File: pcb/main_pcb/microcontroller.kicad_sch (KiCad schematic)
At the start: 33 parts, among them J1 Conn_01x05, J10 Conn_01x06_Male, J11 Conn_01x04, J2 Conn_01x05, J3 Conn_01x05, J4 Conn_01x05, J5 Conn_01x05, J6 Conn_01x05, J7 Conn_01x04, J8 Conn_01x06_Male, J9 Conn_01x04, U1 LSM6DSO, U2 Teensy_4.1, U3 DRV8833

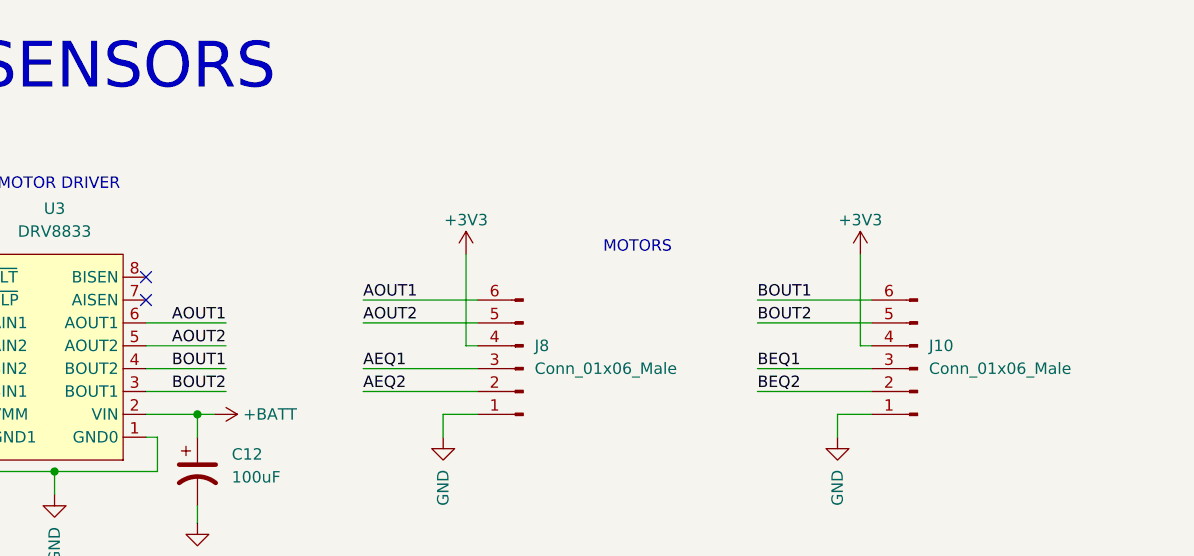
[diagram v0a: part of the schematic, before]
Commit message: Fix many DRC errors; correct motor B sig names
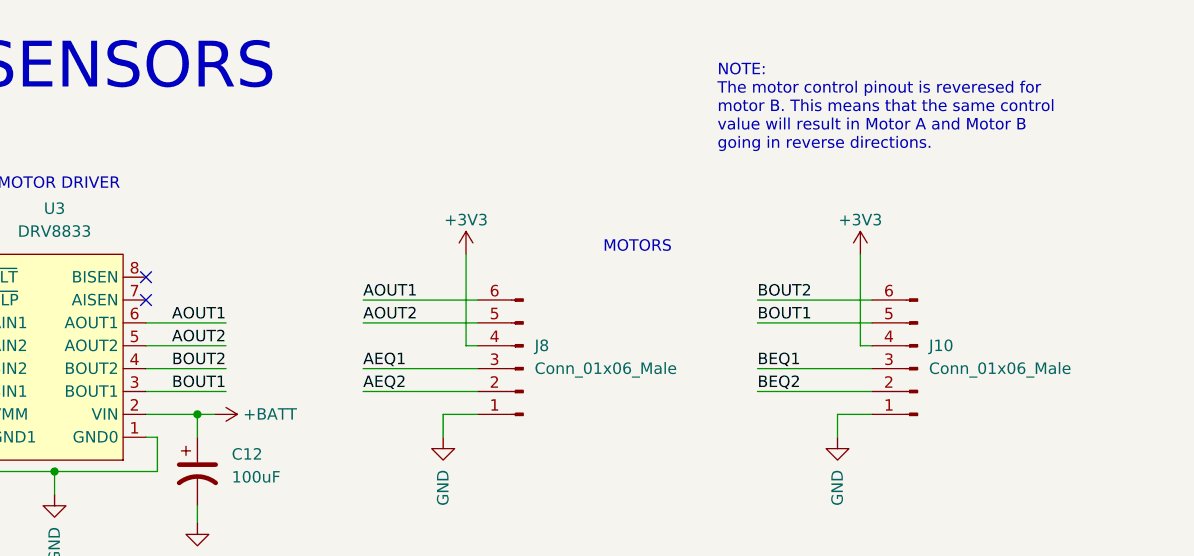
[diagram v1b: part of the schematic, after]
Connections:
- net BOUT1: now also J10.5 (Pin_5), U3.3 (BOUT1); no longer J10.6 (Pin_6), U3.4 (BOUT2)
- net BOUT2: now also J10.6 (Pin_6), U3.4 (BOUT2); no longer J10.5 (Pin_5), U3.3 (BOUT1)
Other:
- note added: "NOTE: The motor control pinout is reveresed for motor B. This means that the same control value will result in Motor A and Motor B going in reverse directions."
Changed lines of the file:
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@@
+    (effects (font (size 1.27 1.27)) (justify left bottom))
+  )
+  (text "NOTE:\nThe motor control pinout is reveresed for\nmotor B. This means that the same control\nvalue will result in Motor A and Motor B\ngoing in reverse directions. "
+    (at 230.505 33.655 0)
     (effects (font (size 1.27 1.27)) (justify left bottom))
   )
@@
     (effects (font (size 1.27 1.27)) (justify left bottom))
   )
-  (label "BOUT1" (at 234.95 50.165 0)
+  (label "BOUT2" (at 234.95 50.165 0)
     (effects (font (size 1.27 1.27)) (justify left bottom))
   )
@@
     (effects (font (size 1.27 1.27)) (justify right bottom))
   )
-  (label "BOUT1" (at 175.895 57.785 180)
+  (label "BOUT2" (at 175.895 57.785 180)
     (effects (font (size 1.27 1.27)) (justify right bottom))
   )
@@
     (effects (font (size 1.27 1.27)) (justify left bottom))
   )
-  (label "BOUT2" (at 234.95 52.705 0)
+  (label "BOUT1" (at 234.95 52.705 0)
     (effects (font (size 1.27 1.27)) (justify left bottom))
   )
@@
     (effects (font (size 1.27 1.27)) (justify right bottom))
   )
-  (label "BOUT2" (at 175.895 60.325 180)
+  (label "BOUT1" (at 175.895 60.325 180)
     (effects (font (size 1.27 1.27)) (justify right bottom))
   )

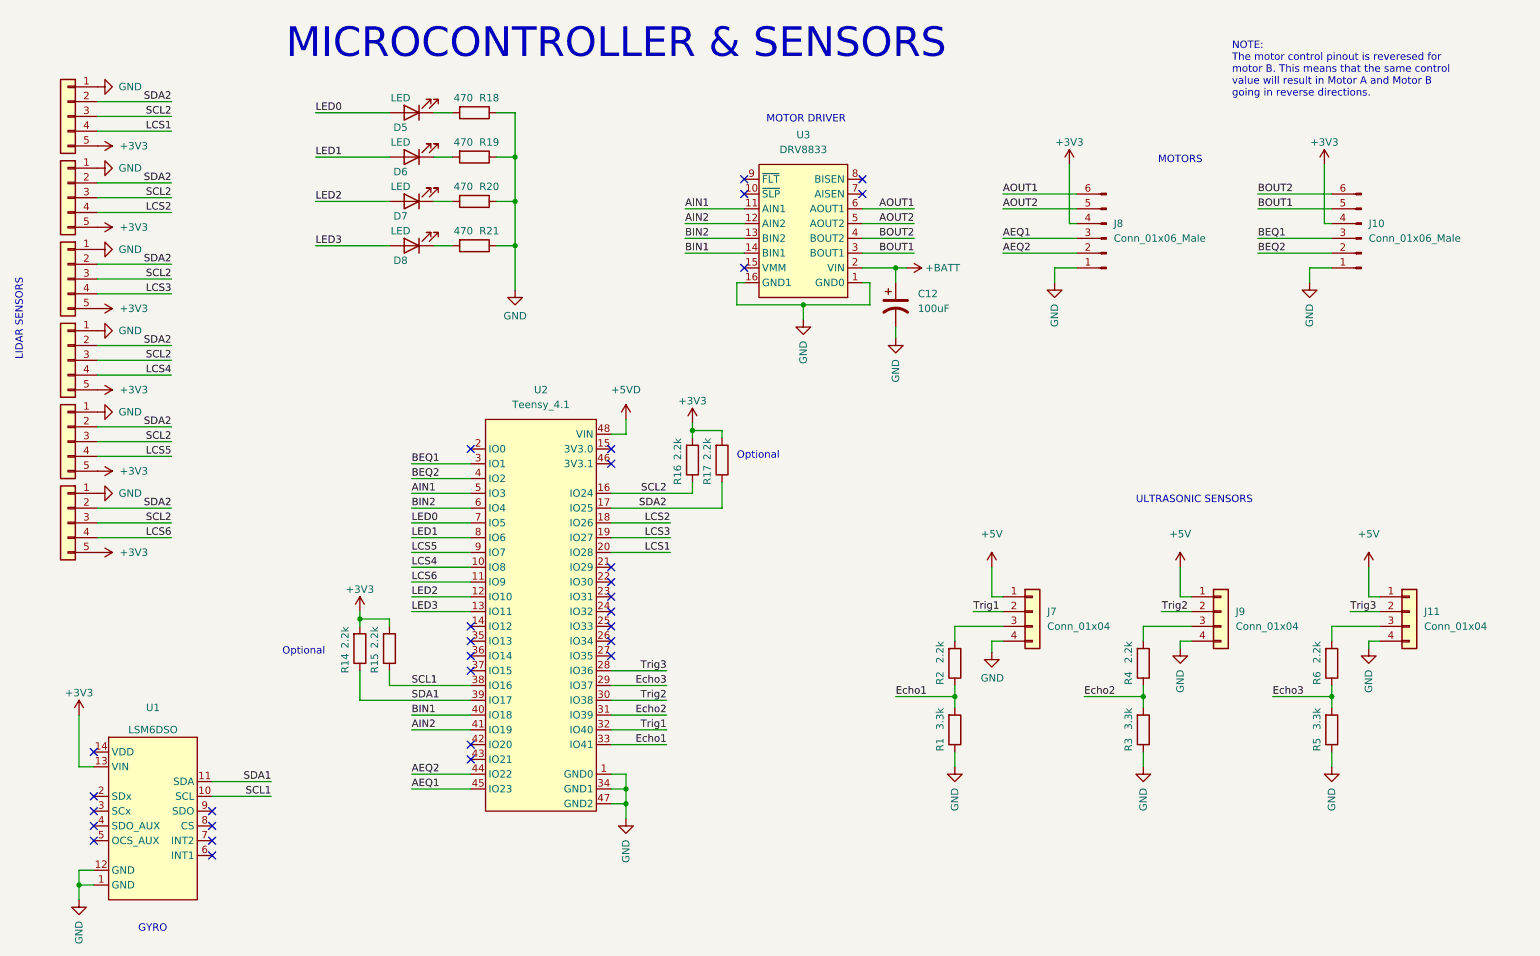
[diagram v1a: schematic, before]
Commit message: Added Teensy 4.0 schematic
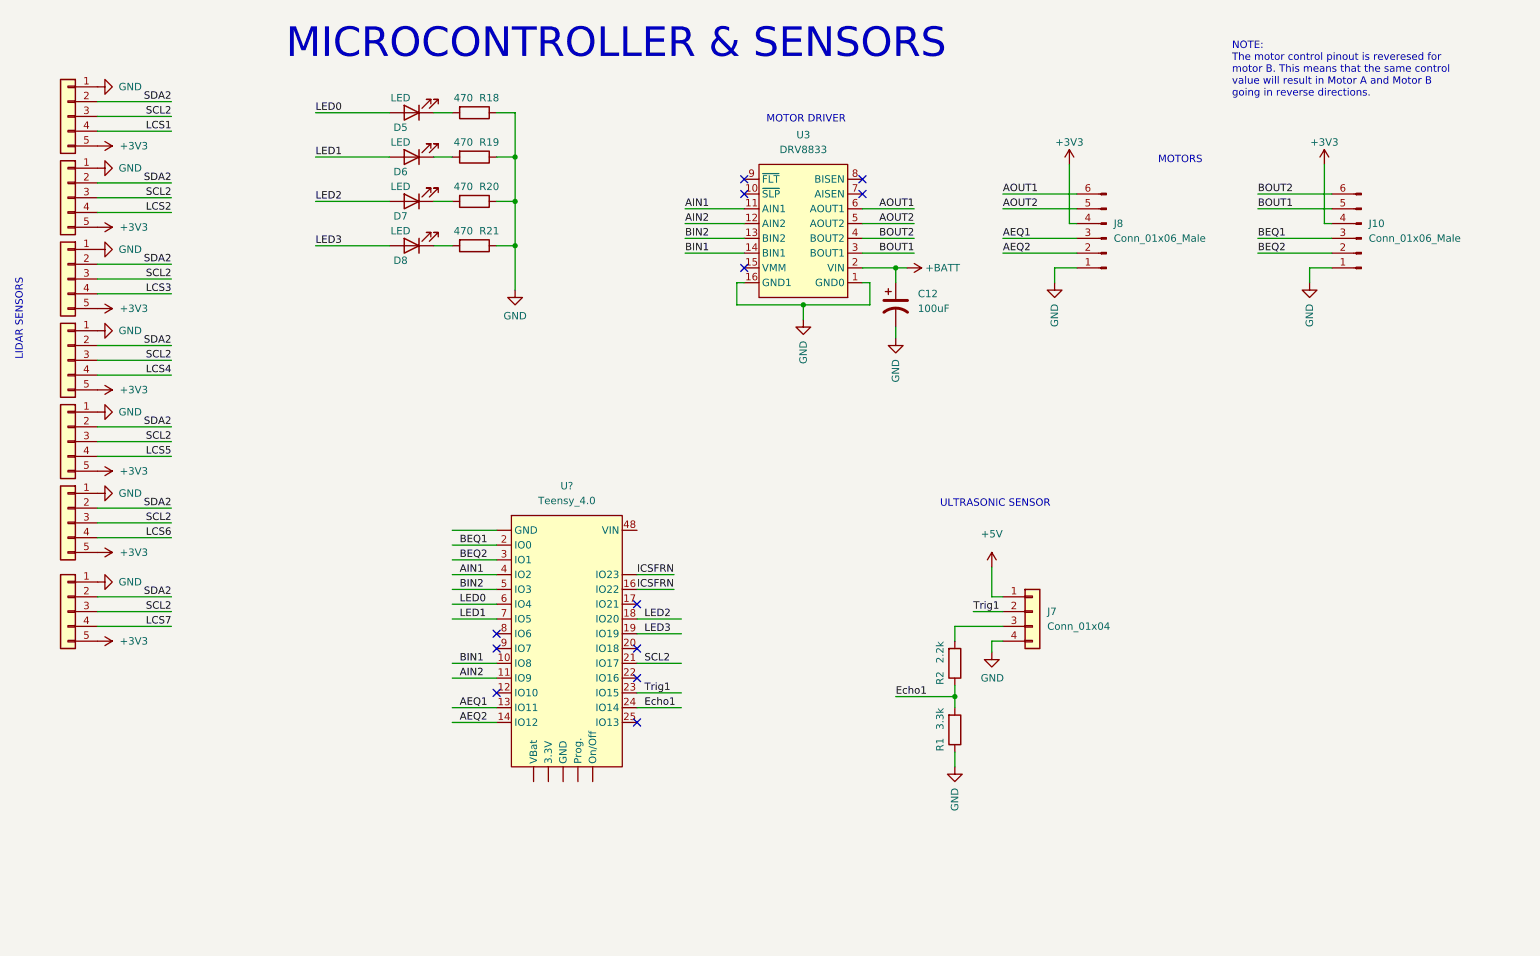
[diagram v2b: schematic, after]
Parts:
- removed J11, J9: Conn_01x04, Connector_JST:JST_XH_B4B-XH-A_1x04_P2.50mm_Vertical, symbol Connector_Generic:Conn_01x04
- removed R14, R15, R16, R17, R4, R6: 2.2k, Resistor_SMD:R_0603_1608Metric_Pad0.98x0.95mm_HandSolder, symbol Device:R
- removed R3, R5: 3.3k, Resistor_SMD:R_0603_1608Metric_Pad0.98x0.95mm_HandSolder, symbol Device:R
- removed U1: LSM6DSO, custom_footprints:SENS_LSM6DSO_Pololu_2798, symbol sym_library:LSM6DSO
- removed U2: Teensy_4.1, custom_footprints:MCU_TEENSY41_PJRC, symbol sym_library:Teensy_4.1
- added J?: Conn_01x05, Connector_JST:JST_XH_B5B-XH-A_1x05_P2.50mm_Vertical, symbol Connector_Generic:Conn_01x05
- added U?: Teensy_4.0, symbol sym_library:Teensy_4.1
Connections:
- net +3V3: now also J?.5 (Pin_5)
- net AEQ1: now also U?.13 (IO11)
- net AEQ2: now also U?.14 (IO12)
- net AIN1: now also U?.4 (IO2)
- net AIN2: now also U?.11 (IO9)
- net BEQ1: now also U?.2 (IO0)
- net BEQ2: now also U?.3 (IO1)
- net BIN1: now also U?.10 (IO8)
- net BIN2: now also U?.5 (IO3)
- net Echo1: now also U?.24 (IO14)
- net GND: now also J?.1 (Pin_1)
- net LED0: now also U?.6 (IO4)
- net LED1: now also U?.7 (IO5)
- net LED2: now also U?.18 (IO20)
- net LED3: now also U?.19 (IO19)
- net SCL2: now also J?.3 (Pin_3), U?.21 (IO17)
- net SDA2: now also J?.2 (Pin_2)
- net Trig1: now also U?.23 (IO15)
- new net ICSFRN: U?. (VBat), U?.16 (IO22)
- new net LCS7: J?.4 (Pin_4)
- no-connect marks 30 -> 12
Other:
- note added: "ULTRASONIC SENSOR"
- note removed: "GYRO"
- note removed: "Optional"
- note removed: "ULTRASONIC SENSORS"
